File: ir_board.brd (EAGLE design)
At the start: 39.9 x 43.4 mm, 13 parts

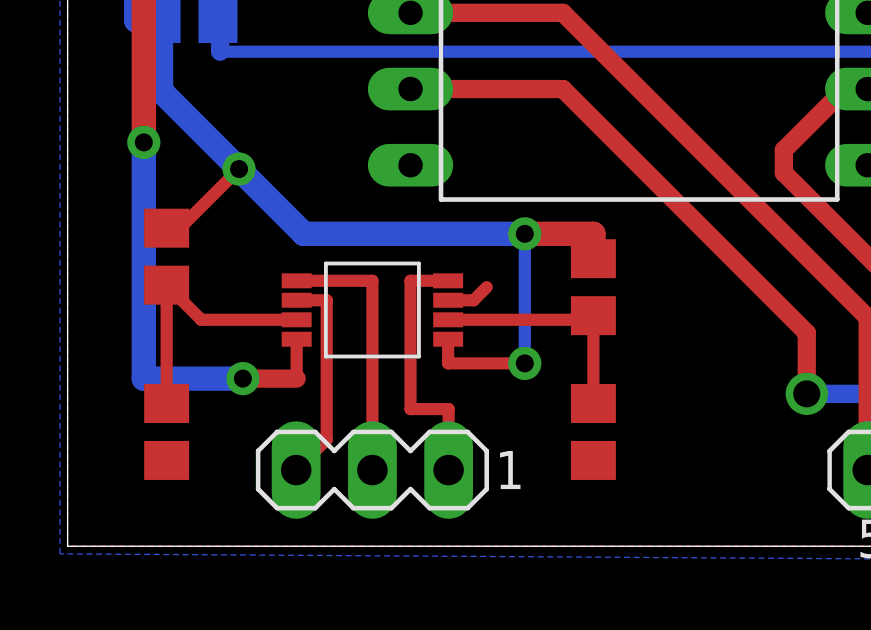
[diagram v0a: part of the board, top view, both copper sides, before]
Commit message: Added debounce caps
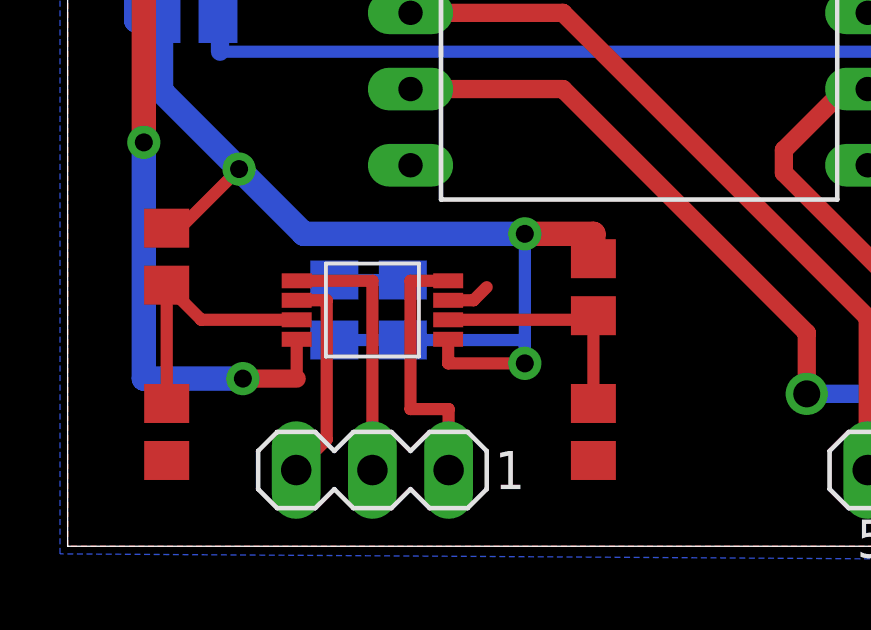
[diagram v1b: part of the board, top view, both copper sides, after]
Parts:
- added C1, C2: (no value), rcl:C0805K
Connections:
- net GND: now also C1.1, C2.1
- net VCC: now also C1.2, C2.2
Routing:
- net VCC: track 130.4 -> 137.6 mm
- net GND: track 1.83 -> 4.11 mm
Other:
- board text added: "Debounce Caps"
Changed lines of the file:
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@@
 2x Pololu QTR-8A
 v. 2013/11/27</text>
+<text x="14.224" y="9.906" size="0.8128" layer="52" rot="MR0">Debounce Caps</text>
 </plain>
 <attributes>
@@
 <element name="R5" library="rcl" package="R0805" value="0ohm" x="17.526" y="3.81" smashed="yes" rot="R270"/>
 <element name="R6" library="rcl" package="R0805" value="0ohm" x="4.064" y="17.526" smashed="yes" rot="MR0"/>
+<element name="C1" library="rcl" package="C0805K" value="" x="11.176" y="7.874" rot="MR270"/>
+<element name="C2" library="rcl" package="C0805K" value="" x="8.89" y="7.874" rot="MR270"/>
 </elements>
 <signals>
@@
 <wire x1="12.685" y1="8.199" x2="13.533" y2="8.199" width="0.4064" layer="1"/>
 <wire x1="13.533" y1="8.199" x2="13.97" y2="8.636" width="0.4064" layer="1"/>
+<contactref element="C1" pad="1"/>
+<contactref element="C2" pad="1"/>
+<wire x1="8.89" y1="8.874" x2="11.176" y2="8.874" width="0.4064" layer="16"/>
 </signal>
 <signal name="VCC" class="1">
@@
 <wire x1="3.744" y1="10.602" x2="5.715" y2="12.573" width="0.4064" layer="1"/>
 <via x="5.715" y="12.573" extent="1-16" drill="0.6"/>
+<contactref element="C1" pad="2"/>
+<contactref element="C2" pad="2"/>
+<wire x1="8.89" y1="6.874" x2="11.176" y2="6.874" width="0.4064" layer="16"/>
+<wire x1="11.176" y1="6.874" x2="15.24" y2="6.874" width="0.4064" layer="16"/>
+<wire x1="15.24" y1="6.874" x2="15.24" y2="6.096" width="0.4064" layer="16"/>
 </signal>
 <signal name="LEDON">

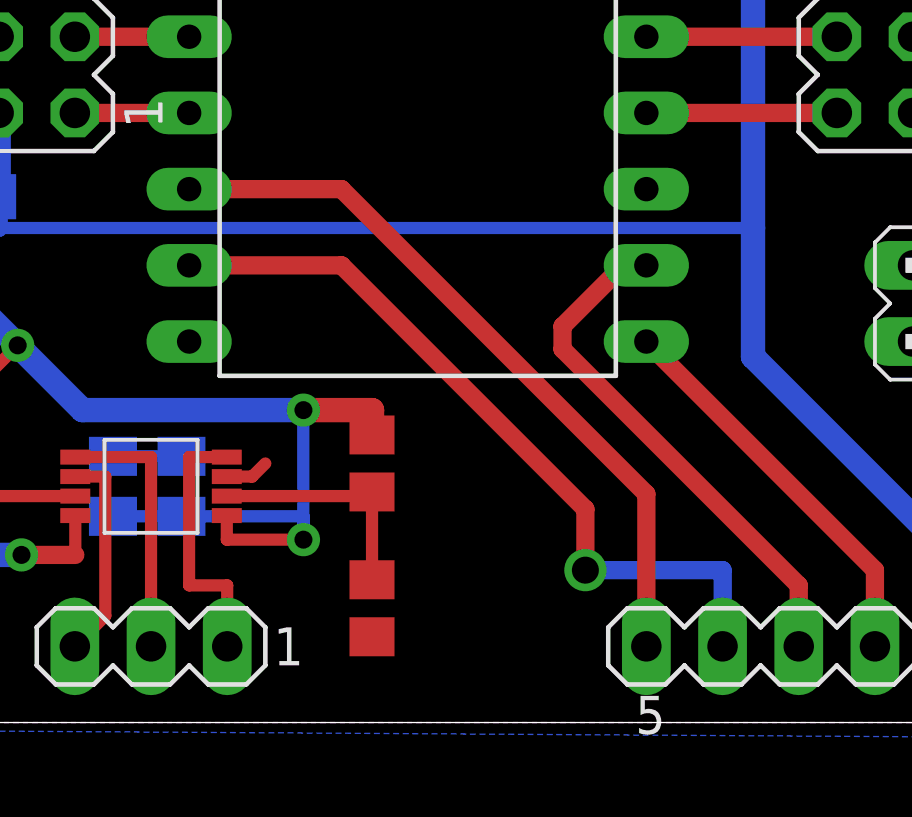
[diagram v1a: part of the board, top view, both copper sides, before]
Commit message: Simplify select line routing and increase clearance
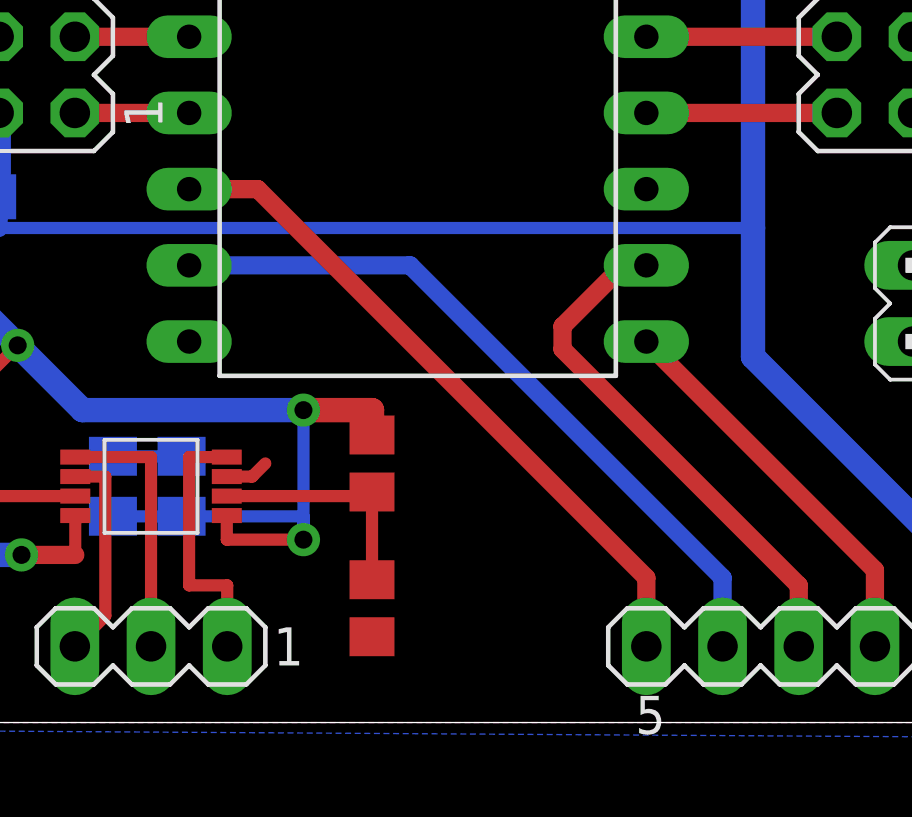
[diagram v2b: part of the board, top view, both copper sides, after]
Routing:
- net A: track 24.5 -> 22.9 mm
- net B: track 25.7 -> 24.4 mm, vias 1 -> 0
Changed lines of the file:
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@@
 <?xml version="1.0" encoding="utf-8"?>
 <!DOCTYPE eagle SYSTEM "eagle.dtd">
-<eagle version="6.5.0">
+<eagle version="6.4">
 <drawing>
 <settings>
@@
 <contactref element="U$2" pad="10"/>
 <contactref element="SV5" pad="5"/>
-<wire x1="26.67" y1="2.54" x2="26.67" y2="7.62" width="0.6096" layer="1"/>
-<wire x1="26.67" y1="7.62" x2="16.51" y2="17.78" width="0.6096" layer="1"/>
-<wire x1="16.51" y1="17.78" x2="11.43" y2="17.78" width="0.6096" layer="1"/>
+<wire x1="26.67" y1="2.54" x2="26.67" y2="4.826" width="0.6096" layer="1"/>
+<wire x1="26.67" y1="4.826" x2="13.716" y2="17.78" width="0.6096" layer="1"/>
+<wire x1="13.716" y1="17.78" x2="11.43" y2="17.78" width="0.6096" layer="1"/>
 </signal>
 <signal name="B">
 <contactref element="U$2" pad="11"/>
 <contactref element="SV5" pad="4"/>
-<wire x1="29.21" y1="2.54" x2="29.21" y2="5.08" width="0.6096" layer="16"/>
-<wire x1="29.21" y1="5.08" x2="24.638" y2="5.08" width="0.6096" layer="16"/>
-<via x="24.638" y="5.08" extent="1-16" drill="0.9"/>
-<wire x1="24.638" y1="5.08" x2="24.638" y2="7.112" width="0.6096" layer="1"/>
-<wire x1="24.638" y1="7.112" x2="16.51" y2="15.24" width="0.6096" layer="1"/>
-<wire x1="16.51" y1="15.24" x2="11.43" y2="15.24" width="0.6096" layer="1"/>
+<wire x1="29.21" y1="2.54" x2="29.21" y2="4.826" width="0.6096" layer="16"/>
+<wire x1="29.21" y1="4.826" x2="18.796" y2="15.24" width="0.6096" layer="16"/>
+<wire x1="18.796" y1="15.24" x2="11.43" y2="15.24" width="0.6096" layer="16"/>
 </signal>
 <signal name="OUT">
